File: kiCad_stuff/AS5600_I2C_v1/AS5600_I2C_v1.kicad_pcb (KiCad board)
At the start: 2 copper layers, 22 x 18.4 mm, 8 parts, among them J1 Conn_01x04, U1 AS5600_ASOM_vEth2

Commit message: That symmetry tho
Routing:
- net SDA: track 18.6 -> 19.7 mm
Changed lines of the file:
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@@
   (segment (start 168.7 80.5) (end 167.845 79.645) (width 0.4) (layer F.Cu) (net 3))
   (segment (start 167.845 79.645) (end 167.845 78.322) (width 0.4) (layer F.Cu) (net 3))
+  (segment (start 169.115 71.747) (end 169.115 72.922) (width 0.4) (layer F.Cu) (net 4))
+  (segment (start 173.028 84.622) (end 174.8 82.85) (width 0.4) (layer F.Cu) (net 4))
+  (segment (start 172.98 84.622) (end 173.028 84.622) (width 0.4) (layer F.Cu) (net 4))
+  (segment (start 174.8 82.85) (end 174.8 74.05) (width 0.4) (layer F.Cu) (net 4))
+  (segment (start 174.8 74.05) (end 171.9 71.15) (width 0.4) (layer F.Cu) (net 4))
+  (segment (start 171.9 71.15) (end 169.712 71.15) (width 0.4) (layer F.Cu) (net 4))
   (segment (start 169.712 71.15) (end 169.115 71.747) (width 0.4) (layer F.Cu) (net 4))
-  (segment (start 171.6 71.15) (end 169.712 71.15) (width 0.4) (layer F.Cu) (net 4))
-  (segment (start 173.75 73.3) (end 171.6 71.15) (width 0.4) (layer F.Cu) (net 4))
-  (segment (start 173.75 82.79134) (end 173.75 73.3) (width 0.4) (layer F.Cu) (net 4))
-  (segment (start 172.98 84.622) (end 172.98 83.56134) (width 0.4) (layer F.Cu) (net 4))
-  (segment (start 172.98 83.56134) (end 173.75 82.79134) (width 0.4) (layer F.Cu) (net 4))
-  (segment (start 169.115 71.747) (end 169.115 72.922) (width 0.4) (layer F.Cu) (net 4))
   (segment (start 167.845 71.747) (end 167.845 72.922) (width 0.4) (layer F.Cu) (net 5))
   (segment (start 167.198 71.1) (end 167.845 71.747) (width 0.4) (layer F.Cu) (net 5))

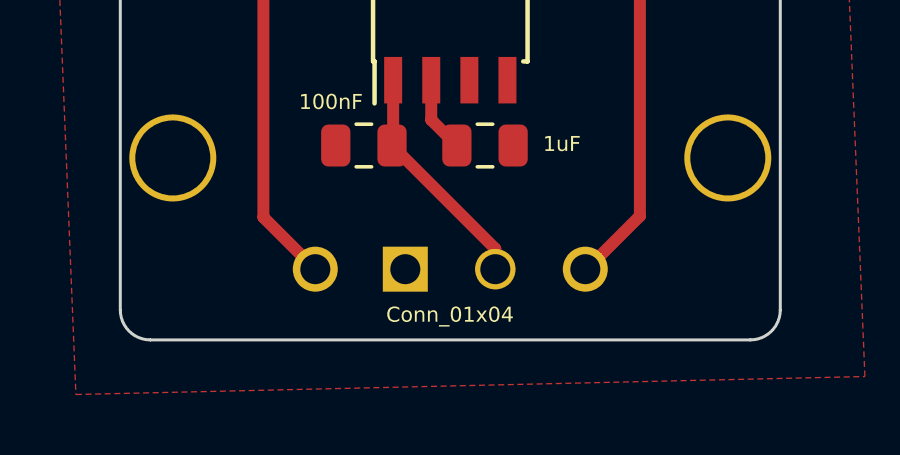
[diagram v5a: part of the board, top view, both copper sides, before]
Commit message: fixed pin text on vEth2
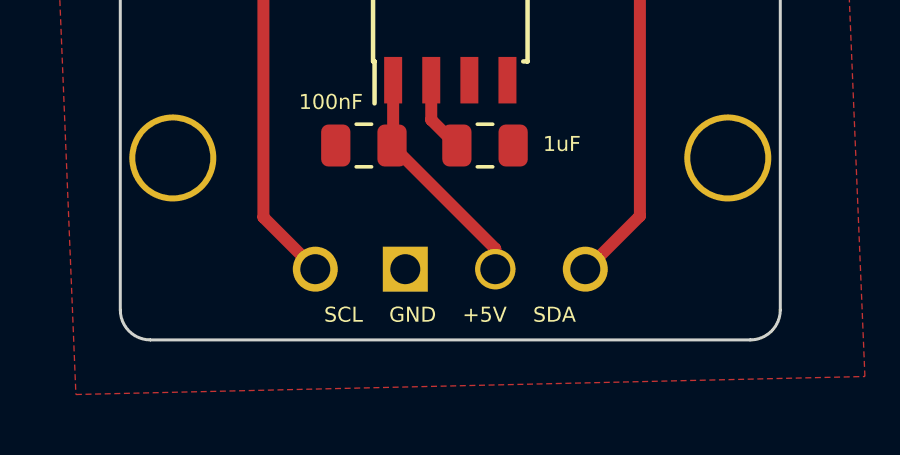
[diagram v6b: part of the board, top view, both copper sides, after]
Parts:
- J1: value Conn_01x04 -> SCL GND +5V SDA
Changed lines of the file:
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@@
       (effects (font (size 1 1) (thickness 0.15)))
     )
-    (fp_text value Conn_01x04 (at -0.01 1.52 180) (layer F.SilkS)
+    (fp_text value "SCL    GND    +5V    SDA" (at -0.01 1.52 180) (layer F.SilkS)
       (effects (font (size 0.5 0.5) (thickness 0.08)))
     )
